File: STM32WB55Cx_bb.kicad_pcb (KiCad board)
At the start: 2 copper layers, 17.8 x 38.1 mm, 33 parts, among them J1 Prog, J2 USB, J3 GPIO1, J4 GPIO2, U1 STM32WB55Cx, U2 LDFM, Y1 LSE, Y2 32MHz

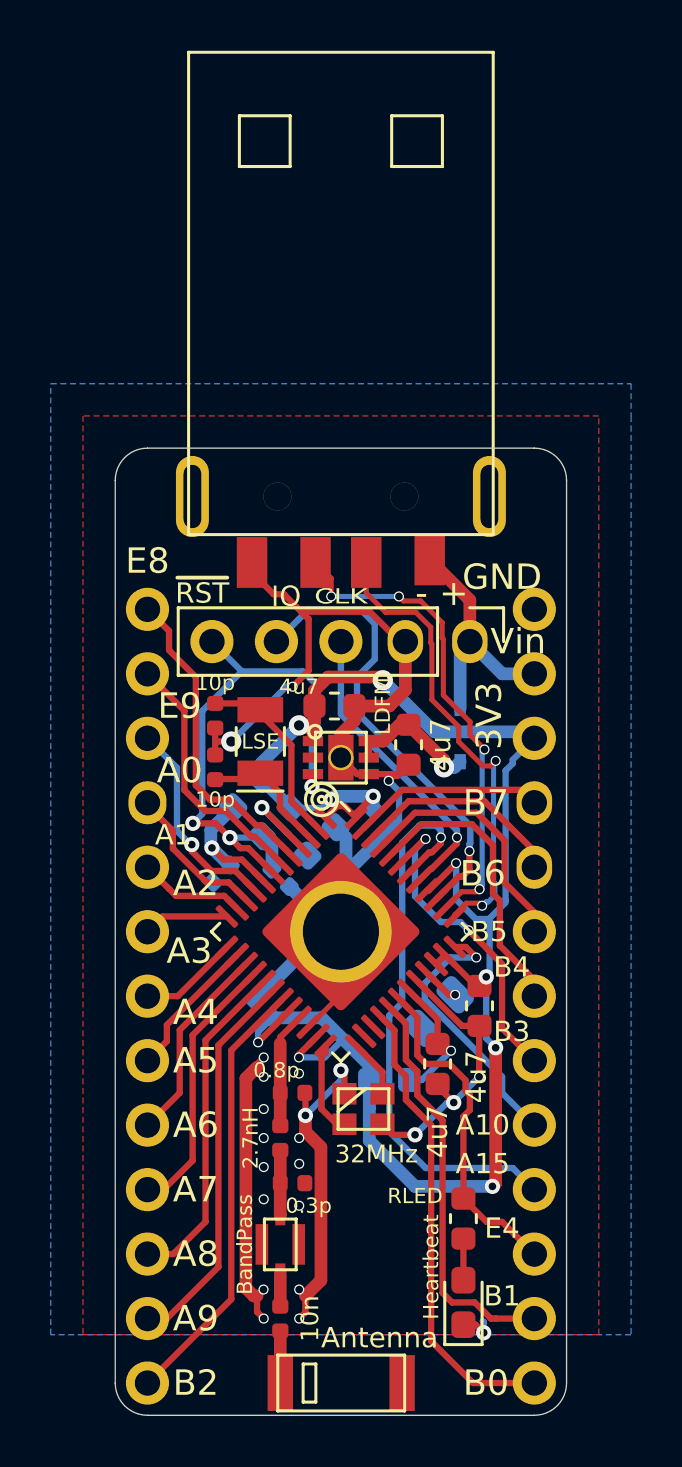
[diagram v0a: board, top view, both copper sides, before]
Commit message: Fix the USB plug so that it's pinout is not reversed. And to avoid changing the board design too much, flip the USB plug to the bottom of the board.
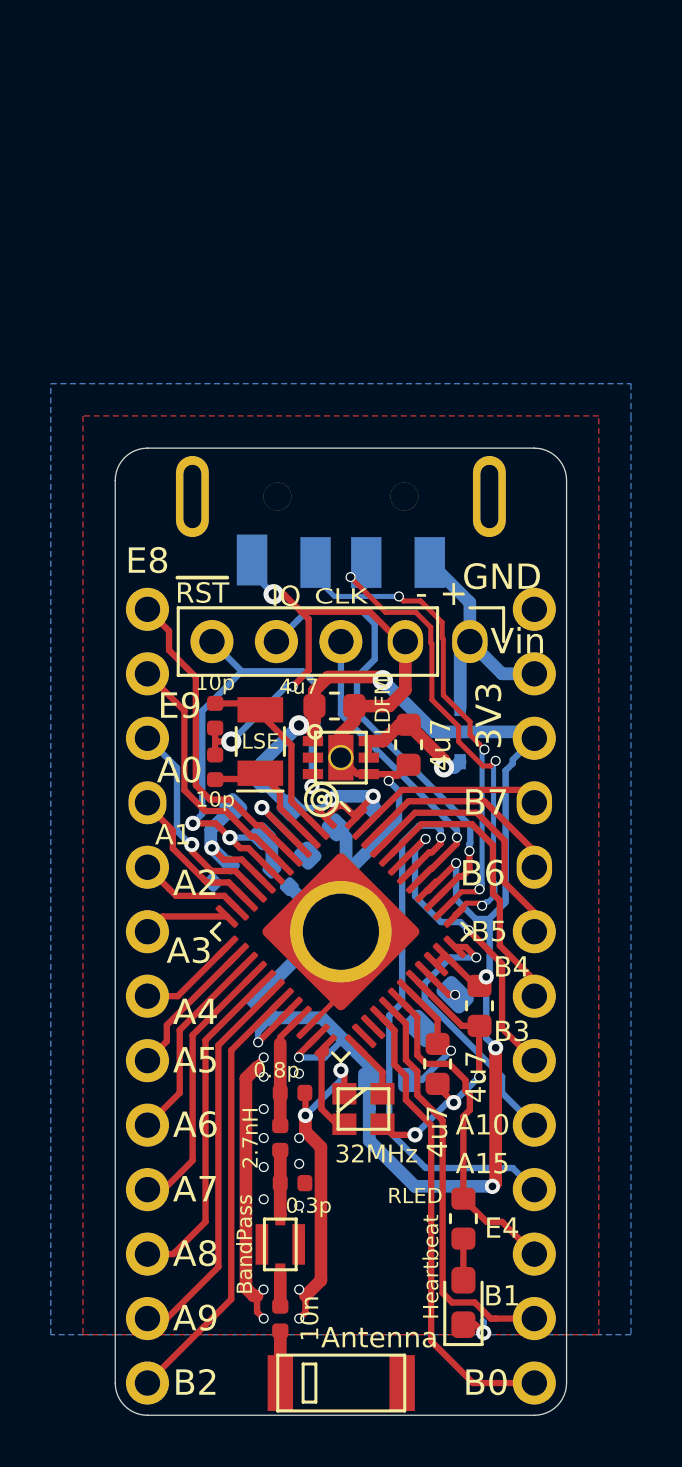
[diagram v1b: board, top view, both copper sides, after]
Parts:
- J2: moved to B.Cu
- turned J2 to 0 degrees
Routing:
- net USB_D-: track 18.6 -> 19.1 mm, vias 2 -> 3
- net GND: track 84.0 -> 84.1 mm, vias 23 -> 24
- net USB_D+: track 19.9 -> 19.8 mm, vias 4 -> 3
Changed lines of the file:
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@@
     (thickness 1.6)
     (drawings 43)
-    (tracks 526)
+    (tracks 530)
     (zones 0)
     (modules 33)
@@
   )
   (setup
-    (last_trace_width 0.25)
+    (last_trace_width 0.5)
     (user_trace_width 0.2)
     (user_trace_width 0.5)
@@
     (add_net ~RST)
   )
+  (module STM32WB55Cx_bb:USBA_Plug_Molex_480372200 (layer B.Cu)
+    (at 210.82 79.375)
+    (fp_text reference J2 (at 0 -3.175) (layer B.Fab)
+      (effects (font (size 1 1) (thickness 0.15)) (justify mirror))
+    )
+    (fp_text value USB (at 0 0.5) (layer B.Fab)
+      (effects (font (size 1 1) (thickness 0.15)) (justify mirror))
+    )
+    (fp_line (start 4 -13) (end 4 -15) (layer B.SilkS) (width 0.12))
+    (fp_line (start 2 -13) (end 4 -13) (layer B.SilkS) (width 0.12))
+    (fp_line (start 2 -15) (end 2 -13) (layer B.SilkS) (width 0.12))
+    (fp_line (start 4 -15) (end 2 -15) (layer B.SilkS) (width 0.12))
+    (fp_line (start -2 -15) (end -4 -15) (layer B.SilkS) (width 0.12))
+    (fp_line (start -2 -13) (end -2 -15) (layer B.SilkS) (width 0.12))
+    (fp_line (start -4 -13) (end -2 -13) (layer B.SilkS) (width 0.12))
+    (fp_line (start -4 -15) (end -4 -13) (layer B.SilkS) (width 0.12))
+    (fp_line (start 6 1.5) (end -6 1.5) (layer B.SilkS) (width 0.12))
+    (fp_line (start 6 -17.5) (end 6 1.5) (layer B.SilkS) (width 0.12))
+    (fp_line (start -6 -17.5) (end 6 -17.5) (layer B.SilkS) (width 0.12))
+    (fp_line (start -6 1.5) (end -6 -17.5) (layer B.SilkS) (width 0.12))
+    (pad 4 smd rect (at -3.5 2.5) (size 1.2 2) (layers B.Cu B.Paste B.Mask)
+      (net 3 GND))
+    (pad 1 smd rect (at 3.5 2.6) (size 1.2 2) (layers B.Cu B.Paste B.Mask)
+      (net 13 VPP))
+    (pad 2 smd rect (at 1 2.6) (size 1.2 2) (layers B.Cu B.Paste B.Mask)
+      (net 16 USB_D-))
+    (pad 3 smd rect (at -1 2.6) (size 1.2 2) (layers B.Cu B.Paste B.Mask)
+      (net 17 USB_D+))
+    (pad 5 thru_hole oval (at 2.5 0) (size 1.1 1.1) (drill 1.1) (layers *.Cu *.Mask)
+      (net 3 GND))
+    (pad 5 thru_hole oval (at -2.5 0) (size 1.1 1.1) (drill 1.1) (layers *.Cu *.Mask)
+      (net 3 GND))
+    (pad 5 thru_hole oval (at 5.85 0) (size 1.3 3.2) (drill oval 0.7 2.5) (layers *.Cu *.Mask)
+      (net 3 GND))
+    (pad 5 thru_hole oval (at -5.85 0) (size 1.3 3.2) (drill oval 0.7 2.5) (layers *.Cu *.Mask)
+      (net 3 GND))
+  )
   (module STM32WB55Cx_bb:oshw_logo (layer B.Cu)
     (at 210.82 108.839 180)
@@
       (net 4 "Net-(C2-Pad2)"))
   )
-  (module STM32WB55Cx_bb:USBA_Plug_Molex_480372200 (layer F.Cu)
-    (at 210.82 79.375 180)
-    (fp_text reference J2 (at 0 3.175) (layer F.Fab)
-      (effects (font (size 1 1) (thickness 0.15)))
-    )
-    (fp_text value USB (at 0 -0.5) (layer F.Fab)
-      (effects (font (size 1 1) (thickness 0.15)))
-    )
-    (fp_line (start -6 -1.5) (end -6 17.5) (layer F.SilkS) (width 0.12))
-    (fp_line (start -6 17.5) (end 6 17.5) (layer F.SilkS) (width 0.12))
-    (fp_line (start 6 17.5) (end 6 -1.5) (layer F.SilkS) (width 0.12))
-    (fp_line (start 6 -1.5) (end -6 -1.5) (layer F.SilkS) (width 0.12))
-    (fp_line (start -4 15) (end -4 13) (layer F.SilkS) (width 0.12))
-    (fp_line (start -4 13) (end -2 13) (layer F.SilkS) (width 0.12))
-    (fp_line (start -2 13) (end -2 15) (layer F.SilkS) (width 0.12))
-    (fp_line (start -2 15) (end -4 15) (layer F.SilkS) (width 0.12))
-    (fp_line (start 4 15) (end 2 15) (layer F.SilkS) (width 0.12))
-    (fp_line (start 2 15) (end 2 13) (layer F.SilkS) (width 0.12))
-    (fp_line (start 2 13) (end 4 13) (layer F.SilkS) (width 0.12))
-    (fp_line (start 4 13) (end 4 15) (layer F.SilkS) (width 0.12))
-    (pad 5 thru_hole oval (at -5.85 0 180) (size 1.3 3.2) (drill oval 0.7 2.5) (layers *.Cu *.Mask)
-      (net 3 GND))
-    (pad 5 thru_hole oval (at 5.85 0 180) (size 1.3 3.2) (drill oval 0.7 2.5) (layers *.Cu *.Mask)
-      (net 3 GND))
-    (pad 5 thru_hole oval (at -2.5 0 180) (size 1.1 1.1) (drill 1.1) (layers *.Cu *.Mask)
-      (net 3 GND))
-    (pad 5 thru_hole oval (at 2.5 0 180) (size 1.1 1.1) (drill 1.1) (layers *.Cu *.Mask)
-      (net 3 GND))
-    (pad 2 smd rect (at -1 -2.6 180) (size 1.2 2) (layers F.Cu F.Paste F.Mask)
-      (net 16 USB_D-))
-    (pad 3 smd rect (at 1 -2.6 180) (size 1.2 2) (layers F.Cu F.Paste F.Mask)
-      (net 17 USB_D+))
-    (pad 4 smd rect (at 3.5 -2.6 180) (size 1.2 2) (layers F.Cu F.Paste F.Mask)
-      (net 3 GND))
-    (pad 1 smd rect (at -3.5 -2.5 180) (size 1.2 2) (layers F.Cu F.Paste F.Mask)
-      (net 13 VPP))
-  )
   (module STM32WB55Cx_bb:QFN-48-1EP_7x7mm_P0.5mm_EP5.3x5.3mm (layer F.Cu)
     (at 210.82 96.52 315)
@@
   (segment (start 210.134106 96.52) (end 210.82 96.52) (width 0.5) (layer B.Cu) (net 3))
   (segment (start 207.429053 99.225053) (end 210.134106 96.52) (width 0.5) (layer B.Cu) (net 3))
-  (segment (start 207.32 82.375) (end 207.32 81.975) (width 0.25) (layer F.Cu) (net 3))
-  (segment (start 208.17 83.225) (end 207.32 82.375) (width 0.25) (layer F.Cu) (net 3))
   (segment (start 208.57 83.225) (end 208.17 83.225) (width 0.25) (layer F.Cu) (net 3))
   (segment (start 213.1165 90.312) (end 213.487 89.9415) (width 0.25) (layer F.Cu) (net 3))
@@
   (segment (start 216.445818 111.89416) (end 216.408 111.856342) (width 0.25) (layer B.Cu) (net 3))
   (segment (start 216.445818 112.318424) (end 216.445818 111.89416) (width 0.25) (layer B.Cu) (net 3))
+  (via (at 208.17 83.225) (size 0.8) (drill 0.4) (layers F.Cu B.Cu) (net 3))
+  (segment (start 207.32 82.375) (end 208.17 83.225) (width 0.25) (layer B.Cu) (net 3))
+  (segment (start 207.32 81.875) (end 207.32 82.375) (width 0.25) (layer B.Cu) (net 3))
   (segment (start 208.4324 106.4236) (end 208.43 106.426) (width 0.5) (layer F.Cu) (net 4))
   (segment (start 208.4324 105.133) (end 208.4324 106.4236) (width 0.5) (layer F.Cu) (net 4))
@@
   (segment (start 217.17 86.36) (end 215.9 85.09) (width 0.5) (layer B.Cu) (net 13))
   (segment (start 218.44 86.36) (end 217.17 86.36) (width 0.5) (layer B.Cu) (net 13))
-  (segment (start 215.9 83.455) (end 215.9 85.09) (width 0.5) (layer F.Cu) (net 13))
-  (segment (start 214.32 81.875) (end 215.9 83.455) (width 0.5) (layer F.Cu) (net 13))
+  (segment (start 215.9 83.555) (end 214.32 81.975) (width 0.5) (layer B.Cu) (net 13))
+  (segment (start 215.9 85.09) (end 215.9 83.555) (width 0.5) (layer B.Cu) (net 13))
   (via (at 215.392 92.80703) (size 0.4) (drill 0.3) (layers F.Cu B.Cu) (net 14))
   (segment (start 215.392 93.043216) (end 215.392 92.80703) (width 0.25) (layer F.Cu) (net 14))
@@
   (segment (start 216.883855 94.605542) (end 216.833854 94.555541) (width 0.2) (layer B.Cu) (net 16))
   (segment (start 216.833854 94.555541) (end 216.833854 91.539359) (width 0.2) (layer B.Cu) (net 16))
-  (segment (start 211.82 83.175) (end 211.82 81.975) (width 0.2) (layer F.Cu) (net 16))
   (segment (start 212.58499 83.93999) (end 211.82 83.175) (width 0.2) (layer F.Cu) (net 16))
   (segment (start 213.774217 83.93999) (end 212.58499 83.93999) (width 0.2) (layer F.Cu) (net 16))
@@
   (segment (start 216.716001 89.988999) (end 216.416799 89.988999) (width 0.2) (layer F.Cu) (net 16))
   (segment (start 216.916 89.789) (end 216.716001 89.988999) (width 0.2) (layer F.Cu) (net 16))
+  (via (at 211.201 82.55) (size 0.4) (drill 0.3) (layers F.Cu B.Cu) (net 16))
+  (segment (start 211.82 83.175) (end 211.201 82.556) (width 0.2) (layer F.Cu) (net 16))
+  (segment (start 211.201 82.556) (end 211.201 82.55) (width 0.2) (layer F.Cu) (net 16))
+  (segment (start 211.245 82.55) (end 211.82 81.975) (width 0.2) (layer B.Cu) (net 16))
+  (segment (start 211.201 82.55) (end 211.245 82.55) (width 0.2) (layer B.Cu) (net 16))
   (segment (start 216.283854 94.945543) (end 216.383854 94.845543) (width 0.2) (layer F.Cu) (net 17))
   (segment (start 214.921219 95.600761) (end 215.576437 94.945543) (width 0.2) (layer F.Cu) (net 17))
   (via (at 216.281 94.845543) (size 0.4) (drill 0.3) (layers F.Cu B.Cu) (net 17))
   (via (at 213.106 83.312) (size 0.4) (drill 0.3) (layers F.Cu B.Cu) (net 17))
-  (via (at 210.439 83.312) (size 0.4) (drill 0.3) (layers F.Cu B.Cu) (net 17))
-  (segment (start 213.106 83.312) (end 210.439 83.312) (width 0.2) (layer B.Cu) (net 17))
-  (segment (start 210.439 82.594) (end 209.82 81.975) (width 0.2) (layer F.Cu) (net 17))
-  (segment (start 210.439 83.312) (end 210.439 82.594) (width 0.2) (layer F.Cu) (net 17))
   (segment (start 216.281 94.845543) (end 216.203543 94.845543) (width 0.2) (layer F.Cu) (net 17))
   (segment (start 216.203543 94.845543) (end 216.103543 94.945543) (width 0.2) (layer F.Cu) (net 17))
@@
   (segment (start 215.906992 88.250607) (end 214.855 87.198615) (width 0.2) (layer F.Cu) (net 17))
   (segment (start 214.855 87.198615) (end 214.855 84.9968) (width 0.2) (layer F.Cu) (net 17))
+  (segment (start 209.82 81.975) (end 209.82 82.566) (width 0.2) (layer B.Cu) (net 17))
+  (segment (start 209.82 82.566) (end 210.566 83.312) (width 0.2) (layer B.Cu) (net 17))
+  (segment (start 213.106 83.312) (end 210.566 83.312) (width 0.2) (layer B.Cu) (net 17))
   (segment (start 208.486548 99.207006) (end 206.502 101.191554) (width 0.25) (layer F.Cu) (net 18))
   (segment (start 206.502 110.998) (end 203.2 114.3) (width 0.25) (layer F.Cu) (net 18))
